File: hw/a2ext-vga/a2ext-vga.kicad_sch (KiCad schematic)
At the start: 13 parts, among them J1 Carrier IDC20, J2 DE-15HD female

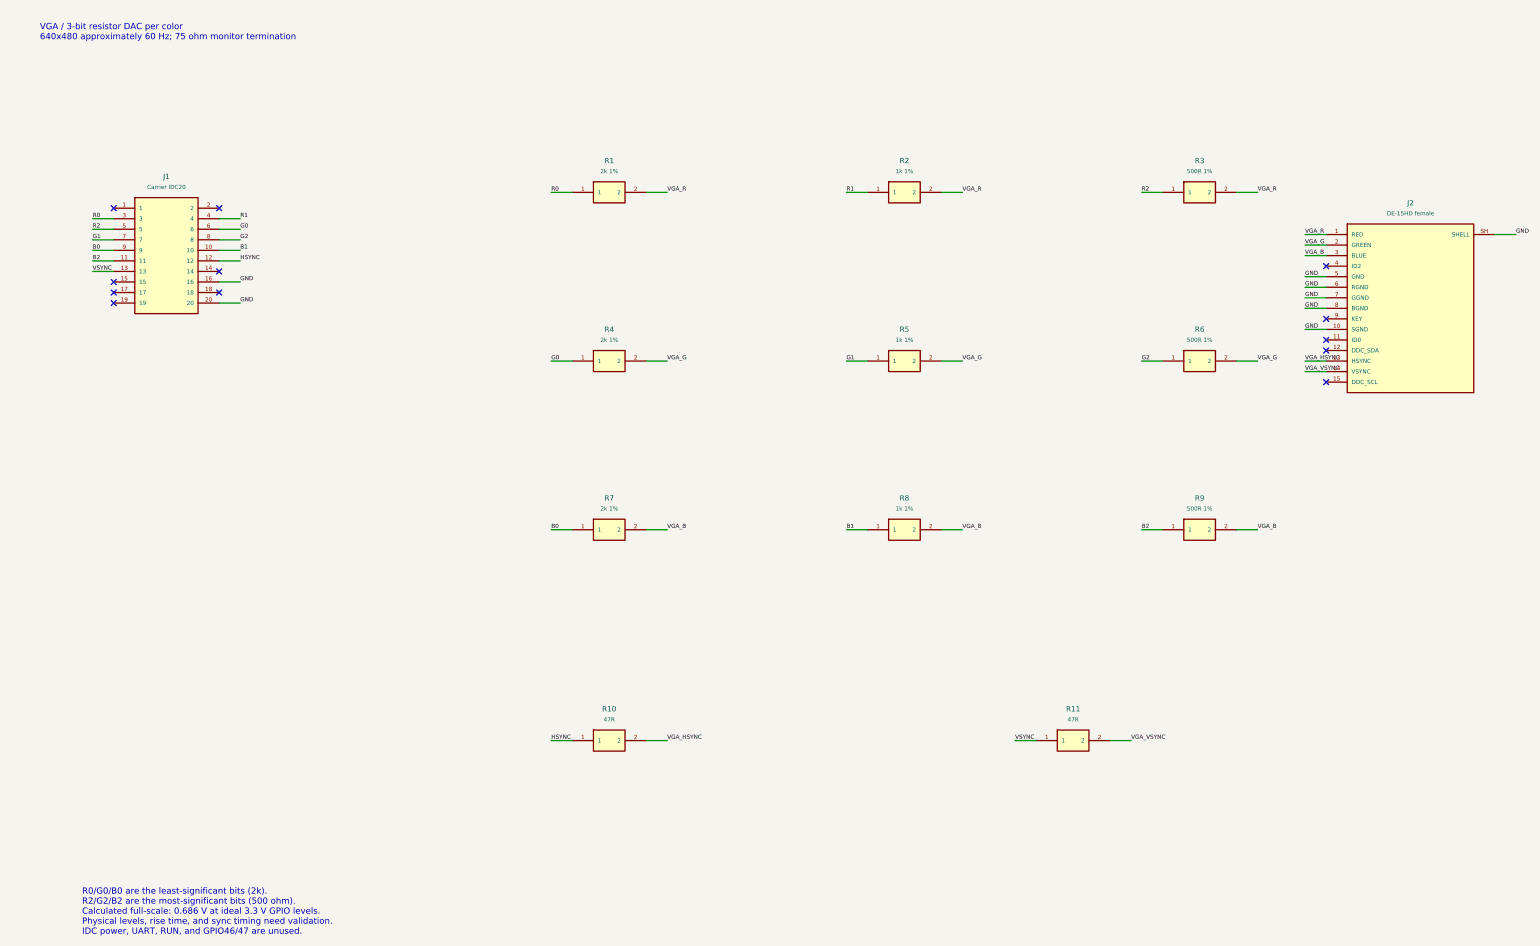
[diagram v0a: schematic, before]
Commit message: Simplify carrier to direct bus and slot power; improve schematic readability
Remove bus isolation and USB power circuitry, clarify signal labels, and reflow all schematics onto A4 landscape with larger text. Update PDFs, BOMs, connectivity checks, operating documentation, progress, and remaining tasks.
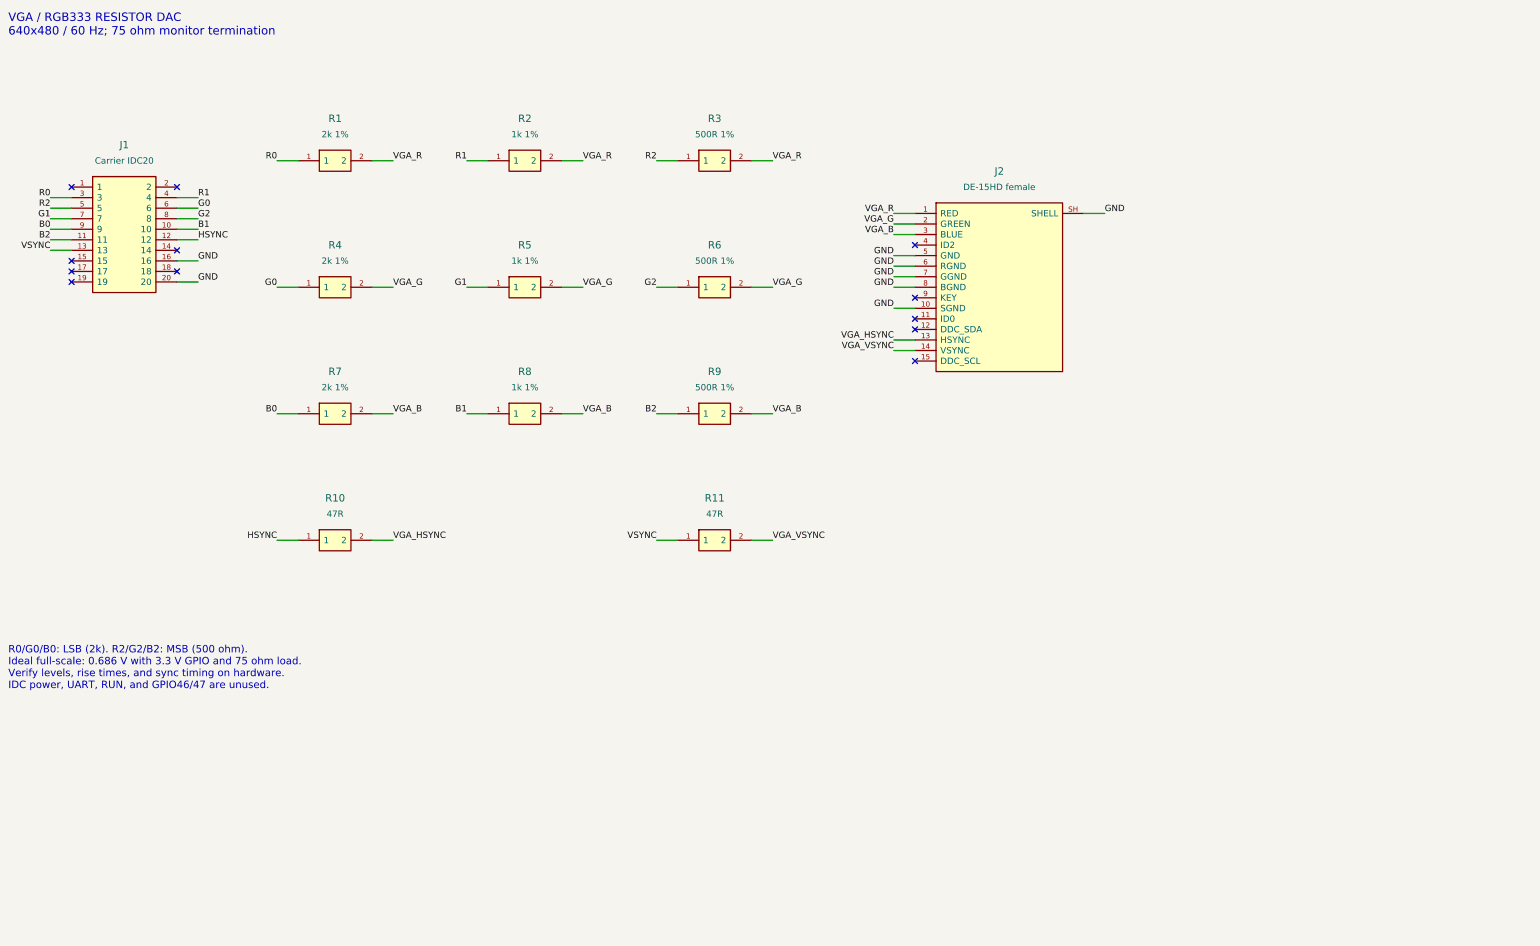
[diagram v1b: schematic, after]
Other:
- note added: "R0/G0/B0: LSB (2k). R2/G2/B2: MSB (500 ohm). Ideal full-scale: 0.686 V with 3.3 V GPIO and 75 ohm load. Verify levels, rise times, and sync timing on hardware. IDC power, UART, RUN, and GPIO46/47 are unused."
- note added: "VGA / RGB333 RESISTOR DAC 640x480 / 60 Hz; 75 ohm monitor termination"
- note removed: "R0/G0/B0 are the least-significant bits (2k). R2/G2/B2 are the most-significant bits (500 ohm). Calculated full-scale: 0.686 V at ideal 3.3 V GPIO levels. Physical levels, rise time, and sync timing need validation. IDC power, UART, RUN, and GPIO46/47 are unused."
- note removed: "VGA / 3-bit resistor DAC per color 640x480 approximately 60 Hz; 75 ohm monitor termination"
- moved on the sheet: J1, J2, R1, R10, R11, R2, R3, R4, R5, R6, R7, R8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

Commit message: Add two-layer prototype PCBs and Gerber packages for all boards
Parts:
- J1: footprint (none) -> A2Ext:Socket20
- J2: footprint (none) -> A2Ext:VGA_DE15
- R1, R10, R11, R2, R3, R4, R5, R6, R7, R8, R9: footprint (none) -> A2Ext:R0805

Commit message: Revise all prototype PCBs for through-hole assembly
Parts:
- R1, R10, R11, R2, R3, R4, R5, R6, R7, R8, R9: footprint A2Ext:R0805 -> A2Ext:R_Axial_7.62
